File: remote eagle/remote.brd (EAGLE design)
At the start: 36.8 x 36.9 mm, 11 parts, among them U1 BLE112-A

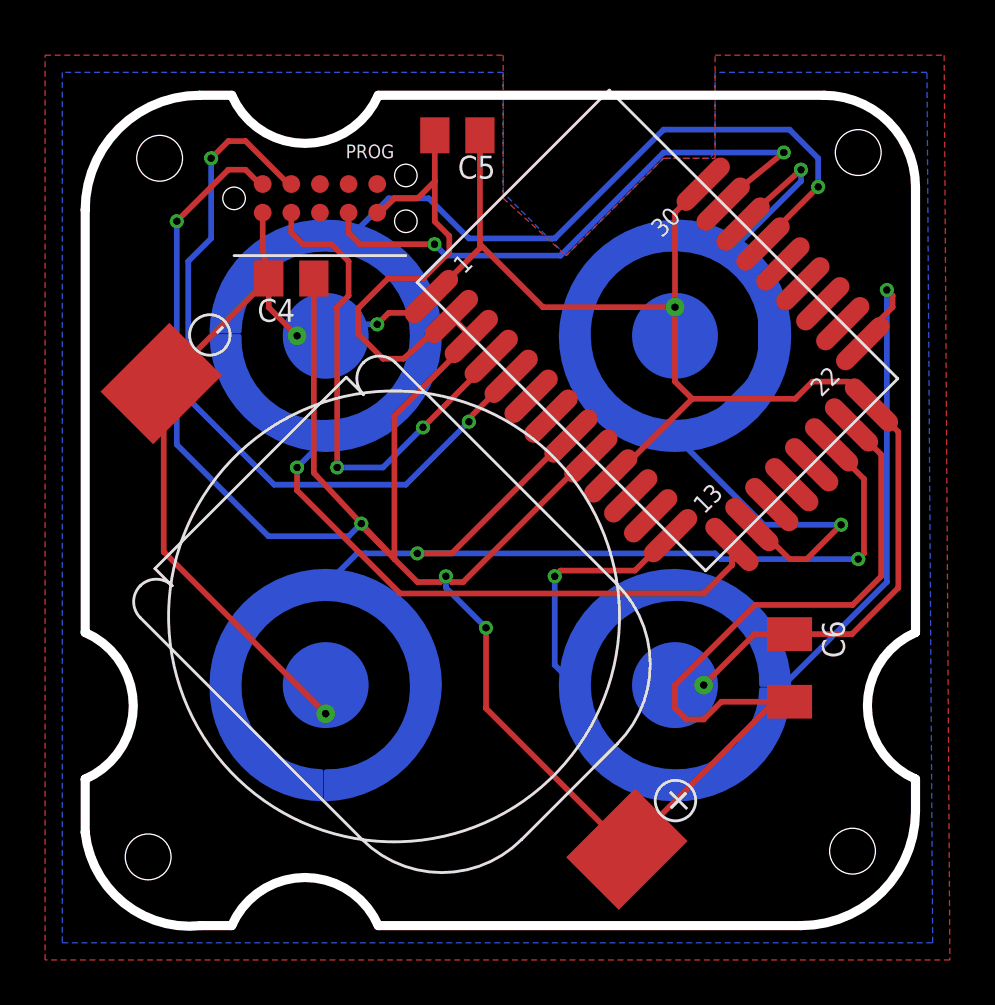
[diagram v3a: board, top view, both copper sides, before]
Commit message: Revision 20 of the pcb. Includes new 6-pin tag connect and nRF51822 Seeed bluetooth module.
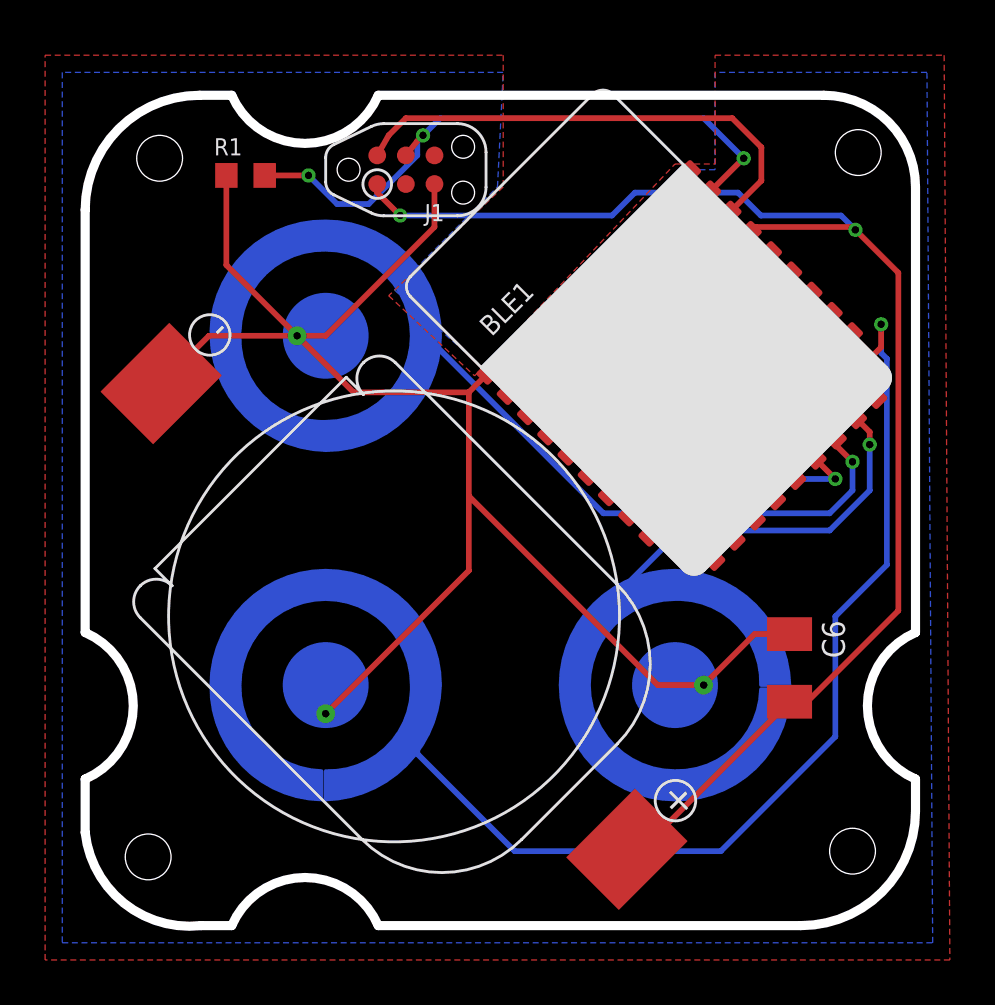
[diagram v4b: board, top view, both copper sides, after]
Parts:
- removed C4, C5: 1uF, resistor:C0805K
- removed PROG: TC2050-MCP-NL, TC2050:TC2030-MCP-NL
- removed U1: BLE112-A, sf-bluegiga:BLE112-A
- added BLE1: BLE Nano, AMLib:SEEED_BLE_MODULE_PAD
- added J1: TC2030-JLINK-NL, connector:TC2030-IDC-NL
- added R1: 10k, resistor:R0603
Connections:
- removed net BUTTON1: U$1.P$3, U1.P0_0, U1.P1_3
- removed net BUTTON2: U$2.P$3, U1.P0_1, U1.P1_4
- removed net BUTTON3: U$3.P$3, U1.P0_6, U1.P1_5
- removed net BUTTON4: U$4.P$3, U1.P0_7, U1.P1_6
- removed net P0_2: U1.P0_2
- removed net P0_3: U1.P0_3
- removed net P0_5: U1.P0_5
- removed net P1_0: U1.P1_0
- removed net P1_1: U1.P1_1
- removed net P1_2: U1.P1_2
- removed net P1_7: U1.P1_7
- removed net P2_0: U1.P2_0
- removed net P2_1: PROG.9, U1.P2_1
- removed net P2_2: PROG.2, U1.P2_2
- removed net RESET: PROG.4, U1.RESET
- removed net SERIAL: U1.P0_4
- removed net USB+: U1.USB+
- removed net USB-: U1.USB-
- new net BLE_SWCLK: BLE1.26, J1.4, R1.2
- new net BLE_SWDIO: BLE1.25, J1.2
- new net P0.00: BLE1.10
- new net P0.01: BLE1.11
- new net P0.02: BLE1.12
- new net P0.03: BLE1.13
- new net P0.04: BLE1.14
- new net P0.05: BLE1.15, U$1.P$3
- new net P0.06: BLE1.16, U$2.P$3
- new net P0.07: BLE1.17, U$3.P$3
- new net P0.08: BLE1.18, U$4.P$3
- new net P0.09: BLE1.19
- new net P0.10: BLE1.20
- new net P0.11: BLE1.21
- new net P0.12: BLE1.22
- new net P0.13: BLE1.23
- new net P0.17: BLE1.3
- new net P0.18: BLE1.2
- new net P0.23: BLE1.4
- new net P0.24: BLE1.5
- new net P0.25: BLE1.6
- new net P0.28: BLE1.7
- new net P0.29: BLE1.8
- new net P0.30: BLE1.9
- net 3.3V: now also BLE1.24, J1.1; no longer C4.1, C5.1, PROG.10, PROG.5, U1.AVDD1, U1.AVDD2, U1.DVDD, U1.VDD_USB
- net GND: now also BLE1.1, BLE1.27, J1.5, R1.1; no longer C4.2, C5.2, PROG.1, U1.GND1, U1.GND2, U1.GND3, U1.GND4
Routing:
- net 3.3V: track 135.4 -> 62.4 mm, vias 4 -> 2
- net BUTTON2: track 68.6 -> 0.00 mm, vias 2 -> 0
- net P0.08: track 0.00 -> 55.1 mm, vias 0 -> 1
- net BUTTON3: track 47.9 -> 0.00 mm, vias 2 -> 0
- net BUTTON4: track 39.0 -> 0.00 mm, vias 2 -> 0
- net P2_1: track 33.7 -> 0.00 mm, vias 2 -> 0
- net BUTTON1: track 33.2 -> 0.00 mm, vias 2 -> 0
- net BLE_SWCLK: track 0.00 -> 28.1 mm, vias 0 -> 3
- net RESET: track 26.1 -> 0.00 mm, vias 2 -> 0
- net P0.06: track 0.00 -> 25.8 mm, vias 0 -> 1
- net P2_2: track 22.3 -> 0.00 mm, vias 2 -> 0
- net BLE_SWDIO: track 0.00 -> 22.2 mm
- net P0.07: track 0.00 -> 21.8 mm, vias 0 -> 1
- net P0.05: track 0.00 -> 9.54 mm, vias 0 -> 1
- net GND: track 102.2 -> 95.3 mm, vias 1 -> 0
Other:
- board text added: "26 June 2015 Rev. 20"
- board text removed: "5 June 2015 Rev. 19"

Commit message: Adding extra corners for snap fit connectors. Beginning to redraw snap fits to accomodate rectangular shape instead of circular shape.
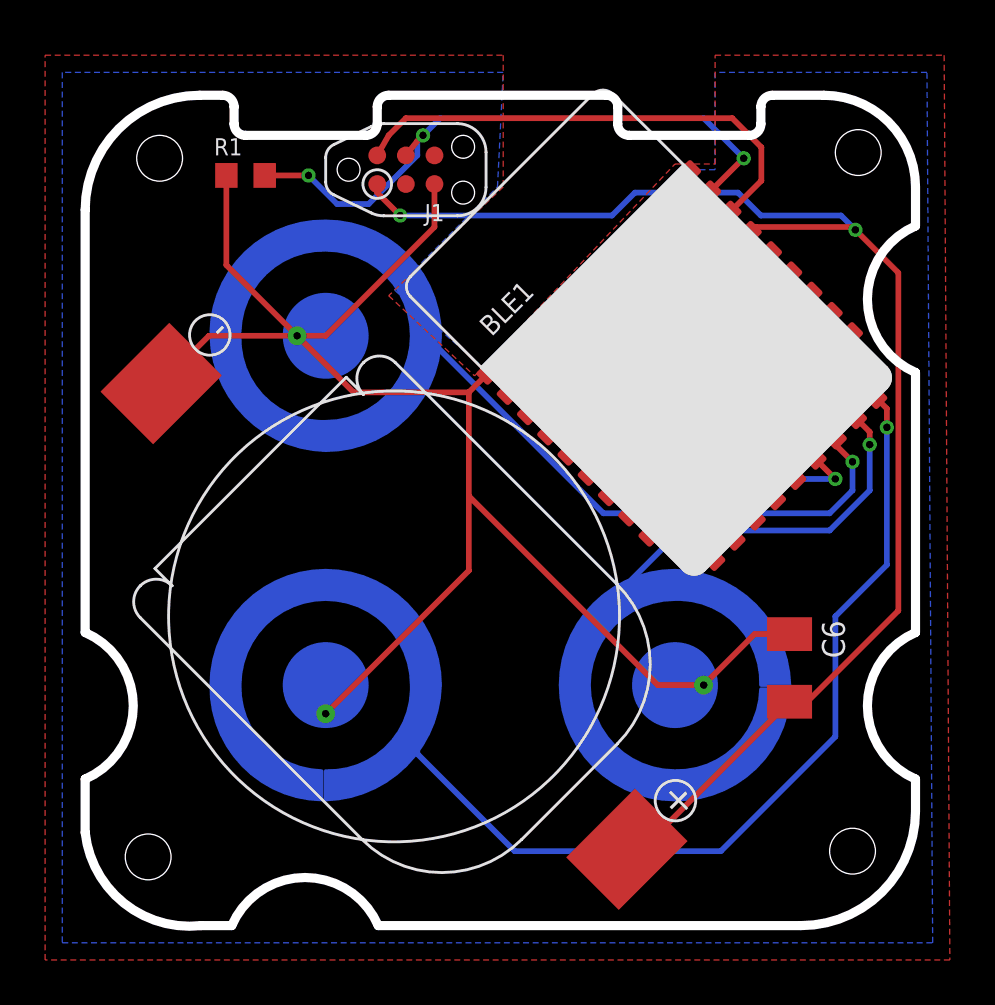
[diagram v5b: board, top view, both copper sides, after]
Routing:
- net P0.08: track 55.1 -> 49.0 mm
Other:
- outline, holes or cut-outs redrawn
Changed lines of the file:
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@@
 <wire x1="31.75" y1="0" x2="36.83" y2="5.08" width="0.4064" layer="20" curve="90"/>
 <wire x1="36.83" y1="5.08" x2="36.83" y2="6.5" width="0.4064" layer="20"/>
-<wire x1="36.83" y1="13" x2="36.83" y2="32.766" width="0.4064" layer="20"/>
+<wire x1="36.83" y1="13" x2="36.83" y2="24.534" width="0.4064" layer="20"/>
+<wire x1="36.83" y1="31.034" x2="36.83" y2="32.766" width="0.4064" layer="20"/>
 <wire x1="36.83" y1="32.766" x2="32.766" y2="36.83" width="0.4064" layer="20" curve="90"/>
-<wire x1="32.766" y1="36.83" x2="13" y2="36.83" width="0.4064" layer="20"/>
-<wire x1="6.5" y1="36.83" x2="5.08" y2="36.83" width="0.4064" layer="20"/>
+<wire x1="32.766" y1="36.83" x2="30.48" y2="36.83" width="0.4064" layer="20"/>
+<wire x1="30.48" y1="36.83" x2="29.972" y2="36.322" width="0.4064" layer="20" curve="90"/>
+<wire x1="29.972" y1="36.322" x2="29.972" y2="35.56" width="0.4064" layer="20"/>
+<wire x1="29.972" y1="35.56" x2="29.464" y2="35.052" width="0.4064" layer="20" curve="-90"/>
+<wire x1="29.464" y1="35.052" x2="24.13" y2="35.052" width="0.4064" layer="20"/>
+<wire x1="24.13" y1="35.052" x2="23.622" y2="35.56" width="0.4064" layer="20" curve="-90"/>
+<wire x1="23.622" y1="35.56" x2="23.622" y2="36.322" width="0.4064" layer="20"/>
+<wire x1="23.622" y1="36.322" x2="23.114" y2="36.83" width="0.4064" layer="20" curve="90"/>
+<wire x1="23.114" y1="36.83" x2="13.462" y2="36.83" width="0.4064" layer="20"/>
+<wire x1="13.462" y1="36.83" x2="12.954" y2="36.322" width="0.4064" layer="20" curve="90"/>
+<wire x1="12.954" y1="36.322" x2="12.954" y2="35.56" width="0.4064" layer="20"/>
+<wire x1="12.954" y1="35.56" x2="12.446" y2="35.052" width="0.4064" layer="20" curve="-90"/>
+<wire x1="7.112" y1="35.052" x2="6.604" y2="35.56" width="0.4064" layer="20" curve="-90"/>
+<wire x1="6.604" y1="36.322" x2="6.096" y2="36.83" width="0.4064" layer="20" curve="90"/>
+<wire x1="6.096" y1="36.83" x2="5.08" y2="36.83" width="0.4064" layer="20"/>
 <wire x1="5.08" y1="36.83" x2="0" y2="31.75" width="0.4064" layer="20" curve="90"/>
 <wire x1="0" y1="13" x2="0" y2="6.5" width="0.4064" layer="20" curve="-133.142614"/>
 <wire x1="6.5" y1="0" x2="13" y2="0" width="0.4064" layer="20" curve="-133.142614"/>
 <wire x1="36.83" y1="6.5" x2="36.83" y2="13" width="0.4064" layer="20" curve="-133.142614"/>
-<wire x1="13" y1="36.83" x2="6.5" y2="36.83" width="0.4064" layer="20" curve="-133.142614"/>
 <wire x1="30.734" y1="30.734" x2="33.02" y2="33.02" width="1.016" layer="22"/>
 <wire x1="31.242" y1="33.02" x2="33.02" y2="33.02" width="1.016" layer="22"/>
 <wire x1="33.02" y1="33.02" x2="33.02" y2="31.242" width="1.016" layer="22"/>
+<wire x1="36.83" y1="24.534" x2="36.83" y2="31.034" width="0.4064" layer="20" curve="-133.142614"/>
+<wire x1="6.604" y1="36.322" x2="6.604" y2="35.56" width="0.4064" layer="20"/>
+<wire x1="7.112" y1="35.052" x2="12.446" y2="35.052" width="0.4064" layer="20"/>
 </plain>
 <attributes>
@@
 <wire x1="34.81869375" y1="23.673509375" x2="34.81869375" y2="23.64269375" width="0.254" layer="1"/>
 <wire x1="34.81869375" y1="23.64269375" x2="34.798" y2="23.622" width="0.254" layer="1"/>
-<wire x1="34.798" y1="23.622" x2="34.798" y2="25.146" width="0.254" layer="1"/>
-<wire x1="34.798" y1="25.146" x2="35.306" y2="25.654" width="0.254" layer="1"/>
-<wire x1="35.306" y1="25.654" x2="35.306" y2="26.67" width="0.254" layer="1"/>
-<via x="35.306" y="26.67" extent="1-16" drill="0.3302"/>
-<wire x1="35.306" y1="26.67" x2="35.306" y2="25.4" width="0.254" layer="16"/>
-<wire x1="35.306" y1="25.4" x2="35.56" y2="25.146" width="0.254" layer="16"/>
-<wire x1="35.56" y1="25.146" x2="35.56" y2="16.002" width="0.254" layer="16"/>
 <wire x1="35.56" y1="16.002" x2="33.274" y2="13.716" width="0.254" layer="16"/>
 <wire x1="33.274" y1="13.716" x2="33.274" y2="8.382" width="0.254" layer="16"/>
@@
 <wire x1="12.446" y1="14.732" x2="11.049" y2="14.732" width="0.254" layer="16"/>
 <wire x1="11.049" y1="14.732" x2="10.668" y2="15.113" width="0.254" layer="16"/>
+<wire x1="35.56" y1="16.002" x2="35.56" y2="22.098" width="0.254" layer="16"/>
+<via x="35.56" y="22.098" extent="1-16" drill="0.3302" shape="octagon"/>
+<wire x1="35.56" y1="22.098" x2="35.56" y2="22.932203125" width="0.254" layer="1"/>
+<wire x1="35.56" y1="22.932203125" x2="34.81869375" y2="23.673509375" width="0.254" layer="1"/>
 </signal>
 <signal name="P0.09">

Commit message: Revision 21 of PCB. Additional snap fit holes, also moved to be symmetric.
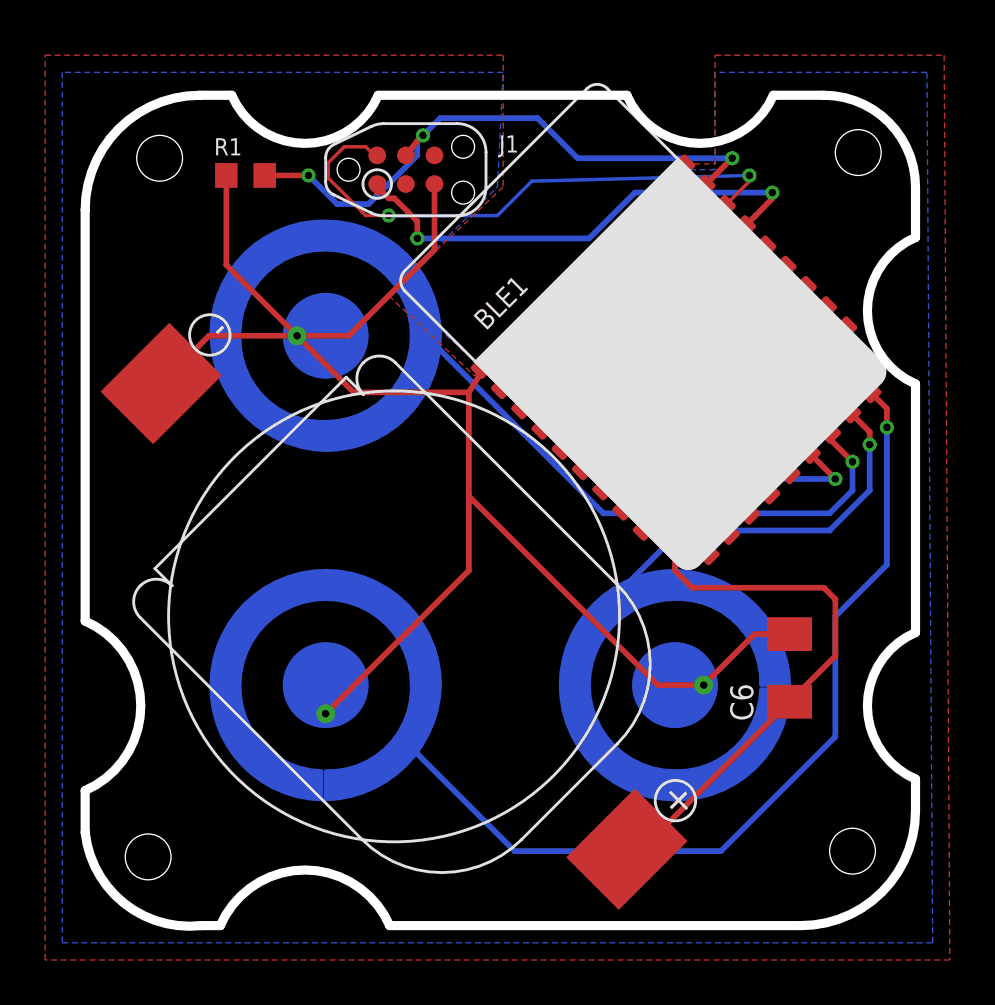
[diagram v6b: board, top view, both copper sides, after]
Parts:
- moved BLE1 0.36 mm to (31.2, 20.1)
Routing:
- net 3.3V: track 62.4 -> 66.8 mm
- net BLE_SWDIO: track 22.2 -> 25.5 mm, vias 0 -> 2
- net GND: track 95.3 -> 96.3 mm
- net BLE_SWCLK: track 28.1 -> 27.2 mm
- net P0.08: track 49.0 -> 49.7 mm
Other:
- outline, holes or cut-outs redrawn
- board text added: "15 July 2015 Rev. 21"
- board text removed: "26 June 2015 Rev. 20"

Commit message: Revision 24 of board. Now uses MDBT40 module.
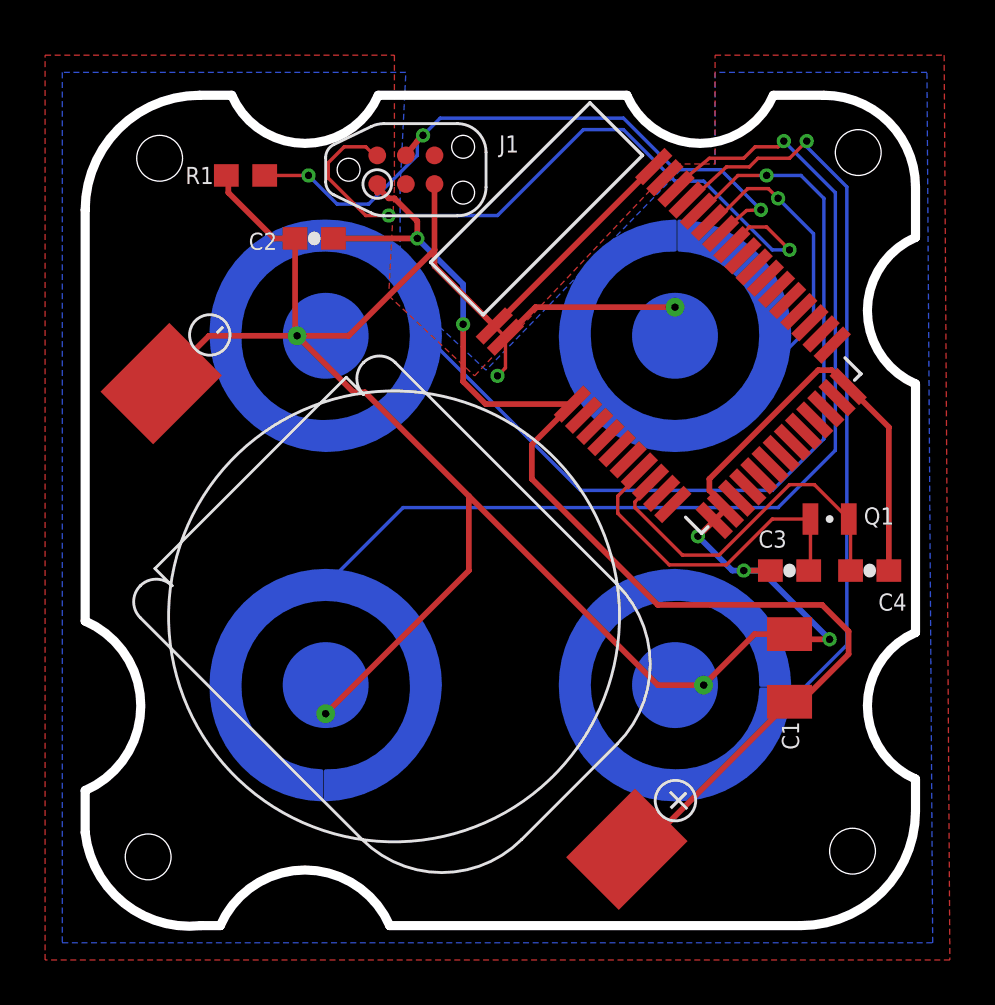
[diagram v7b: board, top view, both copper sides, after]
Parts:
- removed BLE1: BLE Nano, AMLib:SEEED_BLE_MODULE_PAD
- added C2: .1uF, SparkFun-Capacitors:0603-CAP
- added C3, C4: 12.5pF, SparkFun-Capacitors:0603-CAP
- added Q1: FC-12M, crystal:FC-12M
- added U$5: MDBT40SMD, MDBT40:MDBT40
- R1: device resistor:R0603 -> SparkFun-Resistors:0603
- renumbered C6 to C1
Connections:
- removed net P0.00: BLE1.10
- removed net P0.01: BLE1.11
- removed net P0.02: BLE1.12
- removed net P0.03: BLE1.13
- removed net P0.04: BLE1.14
- removed net P0.05: BLE1.15, U$1.P$3
- removed net P0.06: BLE1.16, U$2.P$3
- removed net P0.07: BLE1.17, U$3.P$3
- removed net P0.08: BLE1.18, U$4.P$3
- removed net P0.09: BLE1.19
- removed net P0.10: BLE1.20
- removed net P0.11: BLE1.21
- removed net P0.12: BLE1.22
- removed net P0.13: BLE1.23
- removed net P0.23: BLE1.4
- removed net P0.24: BLE1.5
- removed net P0.25: BLE1.6
- removed net P0.28: BLE1.7
- removed net P0.29: BLE1.8
- removed net P0.30: BLE1.9
- new net C5: C4.1, Q1.2, U$5.10
- new net N$13: C3.1, Q1.1, U$5.9
- new net P0.19: U$3.P$3, U$5.39
- new net P0.20: U$4.P$3, U$5.40
- net 3.3V: now also C2.1, U$5.3; no longer BLE1.24
- net BLE_SWCLK: now also U$5.36; no longer BLE1.26
- net BLE_SWDIO: now also U$5.35; no longer BLE1.25
- net GND: now also C2.2, C3.2, C4.2, U$5.1, U$5.13, U$5.14, U$5.2, U$5.25, U$5.42; no longer BLE1.1, BLE1.27
- net P0.17: now also U$1.P$3, U$5.37; no longer BLE1.3
- net P0.18: now also U$2.P$3, U$5.38; no longer BLE1.2
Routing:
- net P0.08: track 49.7 -> 0.00 mm, vias 1 -> 0
- net P0.19: track 0.00 -> 46.9 mm, vias 0 -> 1
- net P0.20: track 0.00 -> 45.4 mm, vias 0 -> 1
- net P0.18: track 0.00 -> 38.8 mm, vias 0 -> 1
- net GND: track 96.3 -> 131.0 mm, vias 0 -> 4
- net P0.06: track 26.1 -> 0.00 mm, vias 1 -> 0
- net P0.07: track 22.1 -> 0.00 mm, vias 1 -> 0
- net P0.17: track 0.00 -> 18.2 mm, vias 0 -> 1
- net C5: track 0.00 -> 16.0 mm
- net N$13: track 0.00 -> 14.9 mm
- net 3.3V: track 66.8 -> 56.5 mm
- net P0.05: track 9.90 -> 0.00 mm, vias 1 -> 0
- net BLE_SWDIO: track 25.5 -> 31.5 mm
- net BLE_SWCLK: track 27.2 -> 29.5 mm
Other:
- board text added: "23 Aug 2015 Rev. 24"
- board text removed: "15 July 2015 Rev. 21"

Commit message: Revision 28 of the board. Fixing VDD/GND mixup.
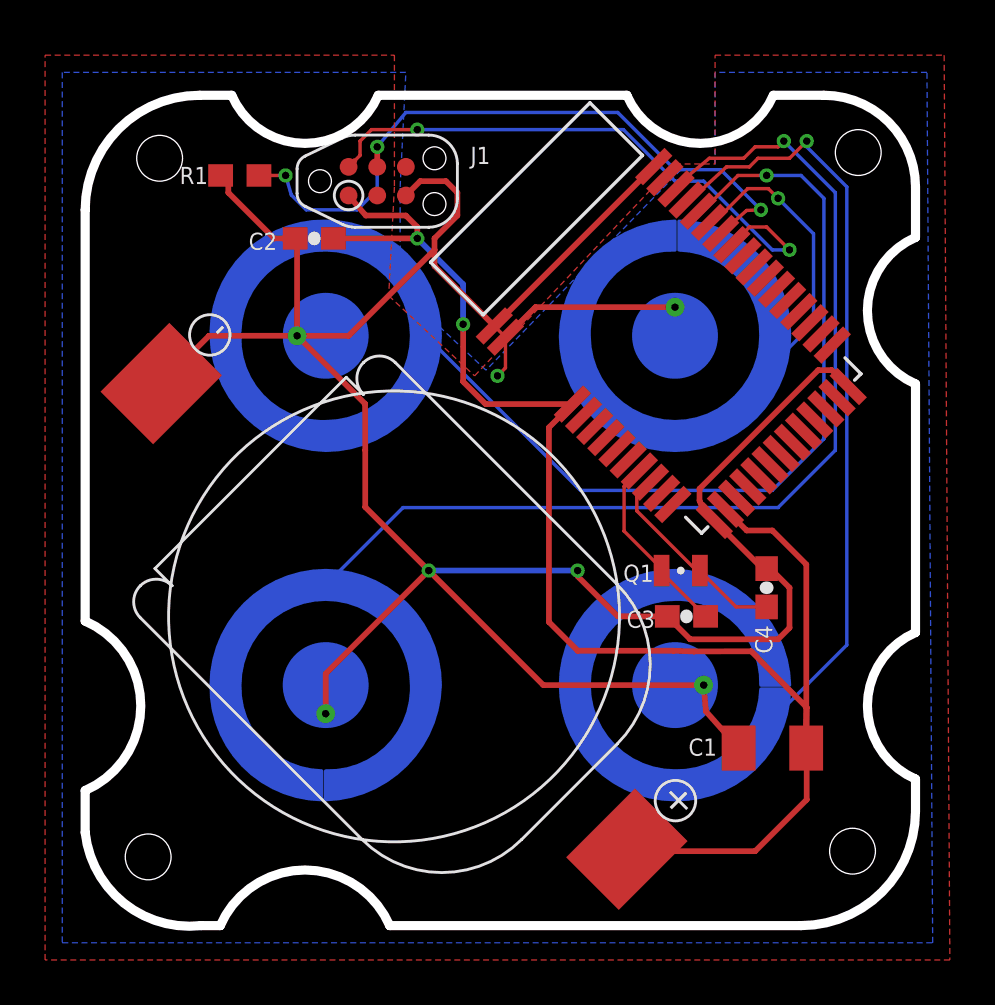
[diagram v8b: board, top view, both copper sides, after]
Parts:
- moved Q1 6.99 mm to (26.4, 15.7)
- moved C3 5.00 mm to (26.7, 13.7)
- moved C4 4.64 mm to (30.2, 15.0), turned to 90 degrees
- moved C1 3.64 mm to (30.5, 7.87), turned to 180 degrees
- moved J1 1.37 mm to (13.0, 33.0)
- moved R1 0.25 mm to (6.86, 33.3)
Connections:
- net 3.3V: now also U$5.14
- net GND: no longer U$5.14
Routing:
- net 3.3V: track 56.5 -> 68.8 mm
- net C5: track 16.0 -> 9.26 mm
- net N$13: track 14.9 -> 8.23 mm
- net BLE_SWDIO: track 31.5 -> 26.1 mm
- net GND: track 131.0 -> 134.5 mm, vias 4 -> 3
- net BLE_SWCLK: track 29.5 -> 31.0 mm
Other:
- board text added: "15 Sept 2015 Rev. 28"
- board text removed: "23 Aug 2015 Rev. 24"
